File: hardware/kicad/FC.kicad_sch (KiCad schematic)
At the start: 0 parts

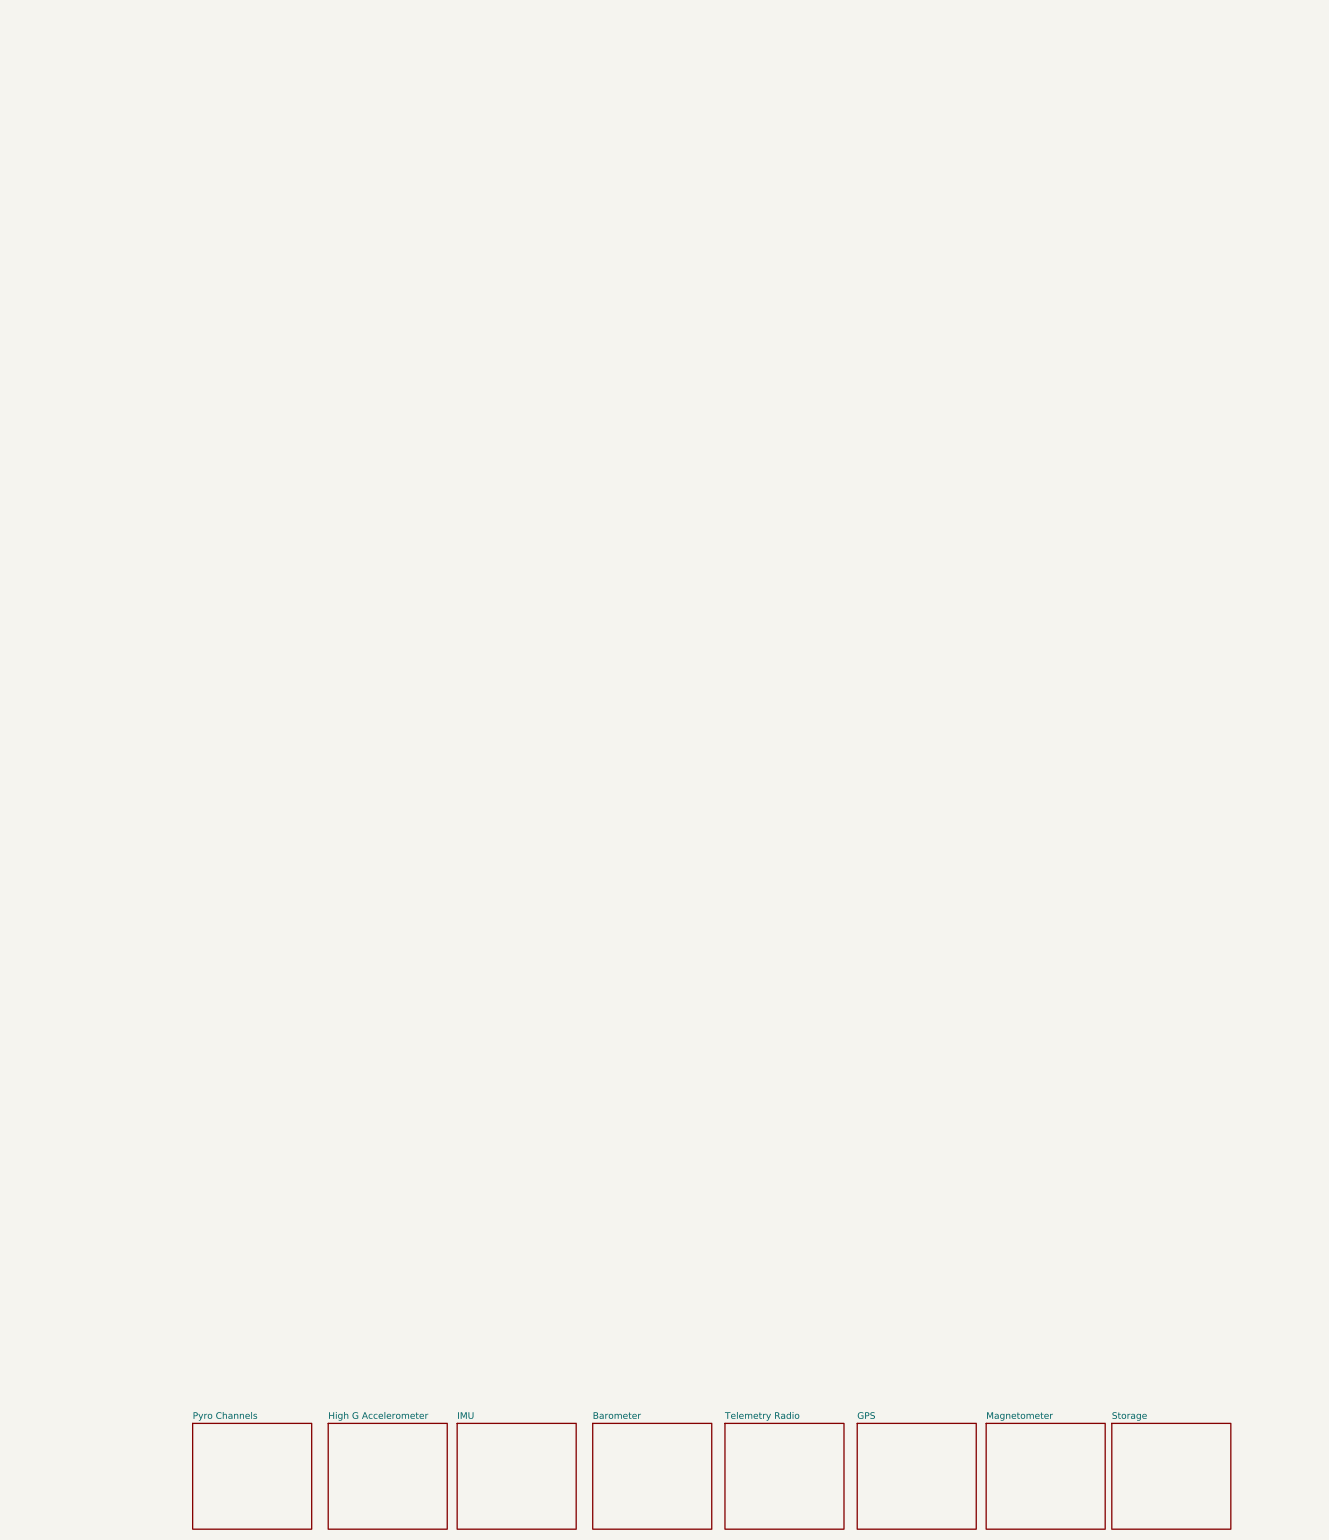
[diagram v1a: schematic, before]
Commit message: created microcontroller schematic
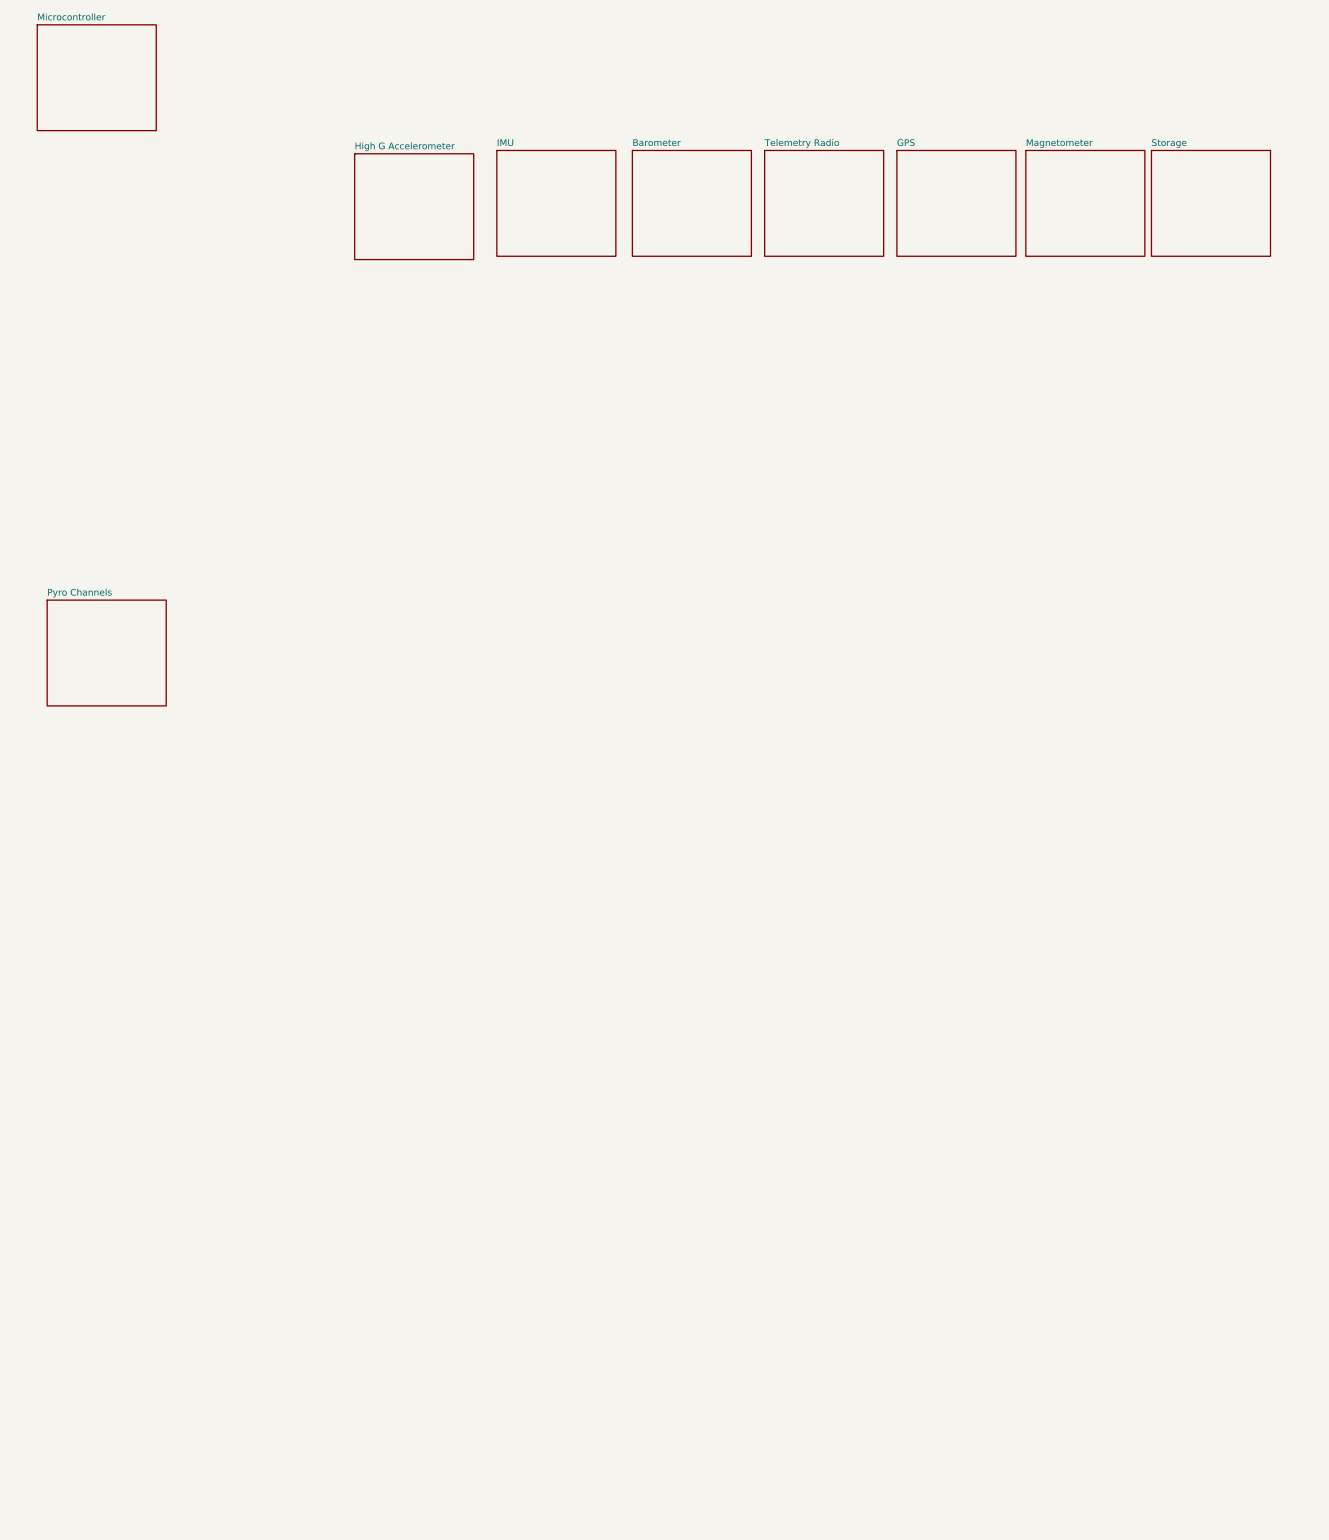
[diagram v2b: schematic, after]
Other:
- added sheet Microcontroller (hierarchical_sheets/atmega32u4.kicad_sch)
- company: (none) -> Missouri S&T Rocket Design Team
- title: (none) -> SRAD-FC
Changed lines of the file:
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@@
 (kicad_sch (version 20230121) (generator eeschema)
-  (paper "A4")
-  (sheet (at 125.095 303.53) (size 22.86 20.32) (fields_autoplaced)
+  (paper "USLetter")
+  (title_block
+    (title "SRAD-FC")
+    (date "2023-09-16")
+    (company "Missouri S&T Rocket Design Team")
+  )
+  (sheet (at 132.715 59.055) (size 22.86 20.32) (fields_autoplaced)
     (stroke (width 0.1524) (type solid))
     (fill (color 255 255 194 1.0000))
-    (property "Sheetname" "Barometer" (at 125.095 302.8184 0)
+    (property "Sheetname" "Barometer" (at 132.715 58.3434 0)
       (effects (font (size 1.27 1.27)) (justify left bottom))
     )
-    (property "Sheetfile" "hierarchical_sheets/ms5611.kicad_sch" (at 125.095 324.4346 0)
+    (property "Sheetfile" "hierarchical_sheets/ms5611.kicad_sch" (at 132.715 79.9596 0)
       (effects (font (size 1.27 1.27)) (justify left top) hide)
     )
@@
     )
   )
-  (sheet (at 48.26 303.53) (size 22.86 20.32) (fields_autoplaced)
+  (sheet (at 20.32 145.415) (size 22.86 20.32) (fields_autoplaced)
     (stroke (width 0.1524) (type solid))
     (fill (color 255 255 194 1.0000))
-    (property "Sheetname" "Pyro Channels" (at 48.26 302.8184 0)
+    (property "Sheetname" "Pyro Channels" (at 20.32 144.7034 0)
       (effects (font (size 1.27 1.27)) (justify left bottom))
     )
-    (property "Sheetfile" "hierarchical_sheets/pyro_channel.kicad_sch" (at 48.26 324.4346 0)
+    (property "Sheetfile" "hierarchical_sheets/pyro_channel.kicad_sch" (at 20.32 166.3196 0)
       (effects (font (size 1.27 1.27)) (justify left top) hide)
     )
@@
     )
   )
-  (sheet (at 150.495 303.53) (size 22.86 20.32) (fields_autoplaced)
+  (sheet (at 158.115 59.055) (size 22.86 20.32) (fields_autoplaced)
     (stroke (width 0.1524) (type solid))
     (fill (color 255 255 194 1.0000))
-    (property "Sheetname" "Telemetry Radio" (at 150.495 302.8184 0)
+    (property "Sheetname" "Telemetry Radio" (at 158.115 58.3434 0)
       (effects (font (size 1.27 1.27)) (justify left bottom))
     )
-    (property "Sheetfile" "hierarchical_sheets/ra-01sh.kicad_sch" (at 150.495 324.4346 0)
+    (property "Sheetfile" "hierarchical_sheets/ra-01sh.kicad_sch" (at 158.115 79.9596 0)
       (effects (font (size 1.27 1.27)) (justify left top) hide)
     )
@@
     )
   )
-  (sheet (at 200.66 303.53) (size 22.86 20.32) (fields_autoplaced)
+  (sheet (at 208.28 59.055) (size 22.86 20.32) (fields_autoplaced)
     (stroke (width 0.1524) (type solid))
     (fill (color 255 255 194 1.0000))
-    (property "Sheetname" "Magnetometer" (at 200.66 302.8184 0)
+    (property "Sheetname" "Magnetometer" (at 208.28 58.3434 0)
       (effects (font (size 1.27 1.27)) (justify left bottom))
     )
-    (property "Sheetfile" "hierarchical_sheets/bmm-350.kicad_sch" (at 200.66 324.4346 0)
+    (property "Sheetfile" "hierarchical_sheets/bmm-350.kicad_sch" (at 208.28 79.9596 0)
       (effects (font (size 1.27 1.27)) (justify left top) hide)
     )
@@
     )
   )
-  (sheet (at 99.06 303.53) (size 22.86 20.32) (fields_autoplaced)
+  (sheet (at 106.68 59.055) (size 22.86 20.32) (fields_autoplaced)
     (stroke (width 0.1524) (type solid))
     (fill (color 255 255 194 1.0000))
-    (property "Sheetname" "IMU" (at 99.06 302.8184 0)
+    (property "Sheetname" "IMU" (at 106.68 58.3434 0)
       (effects (font (size 1.27 1.27)) (justify left bottom))
     )
-    (property "Sheetfile" "hierarchical_sheets/bmi-270.kicad_sch" (at 99.06 324.4346 0)
+    (property "Sheetfile" "hierarchical_sheets/bmi-270.kicad_sch" (at 106.68 79.9596 0)
       (effects (font (size 1.27 1.27)) (justify left top) hide)
     )
@@
     )
   )
-  (sheet (at 74.295 303.53) (size 22.86 20.32) (fields_autoplaced)
+  (sheet (at 18.415 34.925) (size 22.86 20.32) (fields_autoplaced)
     (stroke (width 0.1524) (type solid))
     (fill (color 255 255 194 1.0000))
-    (property "Sheetname" "High G Accelerometer" (at 74.295 302.8184 0)
+    (property "Sheetname" "Microcontroller" (at 18.415 34.2134 0)
       (effects (font (size 1.27 1.27)) (justify left bottom))
     )
-    (property "Sheetfile" "hierarchical_sheets/kx134-1211.kicad_sch" (at 74.295 324.4346 0)
+    (property "Sheetfile" "hierarchical_sheets/atmega32u4.kicad_sch" (at 18.415 55.8296 0)
+      (effects (font (size 1.27 1.27)) (justify left top) hide)
+    )
+    (instances
+      (project "FC"
+        (path "/54cce219-8b98-4e71-96c4-f9ee784aa3bc" (page "10"))
+      )
+    )
+  )
+  (sheet (at 79.375 59.69) (size 22.86 20.32) (fields_autoplaced)
+    (stroke (width 0.1524) (type solid))
+    (fill (color 255 255 194 1.0000))
+    (property "Sheetname" "High G Accelerometer" (at 79.375 58.9784 0)
+      (effects (font (size 1.27 1.27)) (justify left bottom))
+    )
+    (property "Sheetfile" "hierarchical_sheets/kx134-1211.kicad_sch" (at 79.375 80.5946 0)
       (effects (font (size 1.27 1.27)) (justify left top) hide)
     )
@@
     )
   )
-  (sheet (at 224.79 303.53) (size 22.86 20.32) (fields_autoplaced)
+  (sheet (at 232.41 59.055) (size 22.86 20.32) (fields_autoplaced)
     (stroke (width 0.1524) (type solid))
     (fill (color 255 255 194 1.0000))
-    (property "Sheetname" "Storage" (at 224.79 302.8184 0)
+    (property "Sheetname" "Storage" (at 232.41 58.3434 0)
       (effects (font (size 1.27 1.27)) (justify left bottom))
     )
-    (property "Sheetfile" "hierarchical_sheets/mb85rs2mtapnf.kicad_sch" (at 224.79 324.4346 0)
+    (property "Sheetfile" "hierarchical_sheets/mb85rs2mtapnf.kicad_sch" (at 232.41 79.9596 0)
       (effects (font (size 1.27 1.27)) (justify left top) hide)
     )
@@
     )
   )
-  (sheet (at 175.895 303.53) (size 22.86 20.32) (fields_autoplaced)
+  (sheet (at 183.515 59.055) (size 22.86 20.32) (fields_autoplaced)
     (stroke (width 0.1524) (type solid))
     (fill (color 255 255 194 1.0000))
-    (property "Sheetname" "GPS" (at 175.895 302.8184 0)
+    (property "Sheetname" "GPS" (at 183.515 58.3434 0)
       (effects (font (size 1.27 1.27)) (justify left bottom))
     )
-    (property "Sheetfile" "hierarchical_sheets/m10s.kicad_sch" (at 175.895 324.4346 0)
+    (property "Sheetfile" "hierarchical_sheets/m10s.kicad_sch" (at 183.515 79.9596 0)
       (effects (font (size 1.27 1.27)) (justify left top) hide)
     )

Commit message: assigned schematics
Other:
- note added: "Skye: High G Accelerometer - (kx134-1211) Ben: Barometer - (ms5611) Riley: GPS -(m10s) Sean Duda: Magnetometer - (bmm350) Ariel: Telemetry Radio - (Ra-01SH) Clifford: Storage (MB85RS2MTAPNF) Evan: IMU (BMI-270)"
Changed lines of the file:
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@@
     (company "Missouri S&T Rocket Design Team")
   )
-  (sheet (at 132.715 59.055) (size 22.86 20.32) (fields_autoplaced)
+  (text "Skye: High G Accelerometer - (kx134-1211)\nBen: Barometer - (ms5611)\nRiley: GPS -(m10s)\nSean Duda: Magnetometer - (bmm350)\nAriel: Telemetry Radio - (Ra-01SH)\nClifford: Storage (MB85RS2MTAPNF)\nEvan: IMU (BMI-270)\n"
+    (at 158.75 160.02 0)
+    (effects (font (size 2.56 2.56) (thickness 0.512) bold) (justify left bottom))
+  )
+  (sheet (at 127 35.56) (size 22.86 20.32) (fields_autoplaced)
     (stroke (width 0.1524) (type solid))
     (fill (color 255 255 194 1.0000))
-    (property "Sheetname" "Barometer" (at 132.715 58.3434 0)
+    (property "Sheetname" "Barometer" (at 127 34.8484 0)
       (effects (font (size 1.27 1.27)) (justify left bottom))
     )
-    (property "Sheetfile" "hierarchical_sheets/ms5611.kicad_sch" (at 132.715 79.9596 0)
+    (property "Sheetfile" "hierarchical_sheets/ms5611.kicad_sch" (at 127 56.4646 0)
       (effects (font (size 1.27 1.27)) (justify left top) hide)
     )
@@
     )
   )
-  (sheet (at 20.32 145.415) (size 22.86 20.32) (fields_autoplaced)
+  (sheet (at 13.335 172.72) (size 22.86 20.32) (fields_autoplaced)
     (stroke (width 0.1524) (type solid))
     (fill (color 255 255 194 1.0000))
-    (property "Sheetname" "Pyro Channels" (at 20.32 144.7034 0)
+    (property "Sheetname" "Pyro Channels" (at 13.335 172.0084 0)
       (effects (font (size 1.27 1.27)) (justify left bottom))
     )
-    (property "Sheetfile" "hierarchical_sheets/pyro_channel.kicad_sch" (at 20.32 166.3196 0)
+    (property "Sheetfile" "hierarchical_sheets/pyro_channel.kicad_sch" (at 13.335 193.6246 0)
       (effects (font (size 1.27 1.27)) (justify left top) hide)
     )
@@
     )
   )
-  (sheet (at 158.115 59.055) (size 22.86 20.32) (fields_autoplaced)
+  (sheet (at 153.67 34.925) (size 22.86 20.32) (fields_autoplaced)
     (stroke (width 0.1524) (type solid))
     (fill (color 255 255 194 1.0000))
-    (property "Sheetname" "Telemetry Radio" (at 158.115 58.3434 0)
+    (property "Sheetname" "Telemetry Radio" (at 153.67 34.2134 0)
       (effects (font (size 1.27 1.27)) (justify left bottom))
     )
-    (property "Sheetfile" "hierarchical_sheets/ra-01sh.kicad_sch" (at 158.115 79.9596 0)
+    (property "Sheetfile" "hierarchical_sheets/ra-01sh.kicad_sch" (at 153.67 55.8296 0)
       (effects (font (size 1.27 1.27)) (justify left top) hide)
     )
@@
     )
   )
-  (sheet (at 208.28 59.055) (size 22.86 20.32) (fields_autoplaced)
+  (sheet (at 203.835 34.925) (size 22.86 20.32) (fields_autoplaced)
     (stroke (width 0.1524) (type solid))
     (fill (color 255 255 194 1.0000))
-    (property "Sheetname" "Magnetometer" (at 208.28 58.3434 0)
+    (property "Sheetname" "Magnetometer" (at 203.835 34.2134 0)
       (effects (font (size 1.27 1.27)) (justify left bottom))
     )
-    (property "Sheetfile" "hierarchical_sheets/bmm-350.kicad_sch" (at 208.28 79.9596 0)
+    (property "Sheetfile" "hierarchical_sheets/bmm-350.kicad_sch" (at 203.835 55.8296 0)
       (effects (font (size 1.27 1.27)) (justify left top) hide)
     )
@@
     )
   )
-  (sheet (at 106.68 59.055) (size 22.86 20.32) (fields_autoplaced)
+  (sheet (at 102.235 35.56) (size 22.86 20.32) (fields_autoplaced)
     (stroke (width 0.1524) (type solid))
     (fill (color 255 255 194 1.0000))
-    (property "Sheetname" "IMU" (at 106.68 58.3434 0)
+    (property "Sheetname" "IMU" (at 102.235 34.8484 0)
       (effects (font (size 1.27 1.27)) (justify left bottom))
     )
-    (property "Sheetfile" "hierarchical_sheets/bmi-270.kicad_sch" (at 106.68 79.9596 0)
+    (property "Sheetfile" "hierarchical_sheets/bmi-270.kicad_sch" (at 102.235 56.4646 0)
       (effects (font (size 1.27 1.27)) (justify left top) hide)
     )
@@
     )
   )
-  (sheet (at 79.375 59.69) (size 22.86 20.32) (fields_autoplaced)
+  (sheet (at 78.105 35.56) (size 22.86 20.32) (fields_autoplaced)
     (stroke (width 0.1524) (type solid))
     (fill (color 255 255 194 1.0000))
-    (property "Sheetname" "High G Accelerometer" (at 79.375 58.9784 0)
+    (property "Sheetname" "High G Accelerometer" (at 78.105 34.8484 0)
       (effects (font (size 1.27 1.27)) (justify left bottom))
     )
-    (property "Sheetfile" "hierarchical_sheets/kx134-1211.kicad_sch" (at 79.375 80.5946 0)
+    (property "Sheetfile" "hierarchical_sheets/kx134-1211.kicad_sch" (at 78.105 56.4646 0)
       (effects (font (size 1.27 1.27)) (justify left top) hide)
     )
@@
     )
   )
-  (sheet (at 232.41 59.055) (size 22.86 20.32) (fields_autoplaced)
+  (sheet (at 230.505 34.925) (size 22.86 20.32) (fields_autoplaced)
     (stroke (width 0.1524) (type solid))
     (fill (color 255 255 194 1.0000))
-    (property "Sheetname" "Storage" (at 232.41 58.3434 0)
+    (property "Sheetname" "Storage" (at 230.505 34.2134 0)
       (effects (font (size 1.27 1.27)) (justify left bottom))
     )
-    (property "Sheetfile" "hierarchical_sheets/mb85rs2mtapnf.kicad_sch" (at 232.41 79.9596 0)
+    (property "Sheetfile" "hierarchical_sheets/mb85rs2mtapnf.kicad_sch" (at 230.505 55.8296 0)
       (effects (font (size 1.27 1.27)) (justify left top) hide)
     )
@@
     )
   )
-  (sheet (at 183.515 59.055) (size 22.86 20.32) (fields_autoplaced)
+  (sheet (at 179.07 34.925) (size 22.86 20.32) (fields_autoplaced)
     (stroke (width 0.1524) (type solid))
     (fill (color 255 255 194 1.0000))
-    (property "Sheetname" "GPS" (at 183.515 58.3434 0)
+    (property "Sheetname" "GPS" (at 179.07 34.2134 0)
       (effects (font (size 1.27 1.27)) (justify left bottom))
     )
-    (property "Sheetfile" "hierarchical_sheets/m10s.kicad_sch" (at 183.515 79.9596 0)
+    (property "Sheetfile" "hierarchical_sheets/m10s.kicad_sch" (at 179.07 55.8296 0)
       (effects (font (size 1.27 1.27)) (justify left top) hide)
     )

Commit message: Storage Updated
Didn't save. Added pins to hierarchal sheets. In/Out
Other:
- sheet Storage ports: added SCK, SI, SO, ~{CS}, ~{HOLD}, ~{WP}; removed none
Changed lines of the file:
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@@
     )
   )
-  (sheet (at 230.505 34.925) (size 22.86 20.32) (fields_autoplaced)
+  (sheet (at 237.49 34.925) (size 18.415 20.955) (fields_autoplaced)
     (stroke (width 0.1524) (type solid))
     (fill (color 255 255 194 1.0000))
-    (property "Sheetname" "Storage" (at 230.505 34.2134 0)
+    (property "Sheetname" "Storage" (at 237.49 34.2134 0)
       (effects (font (size 1.27 1.27)) (justify left bottom))
     )
-    (property "Sheetfile" "hierarchical_sheets/mb85rs2mtapnf.kicad_sch" (at 230.505 55.8296 0)
+    (property "Sheetfile" "hierarchical_sheets/mb85rs2mtapnf.kicad_sch" (at 237.49 56.4646 0)
       (effects (font (size 1.27 1.27)) (justify left top) hide)
     )
+    (pin "SCK" input (at 255.905 38.1 0)
+      (effects (font (size 1.27 1.27)) (justify right))
+    )
+    (pin "SO" output (at 237.49 45.72 180)
+      (effects (font (size 1.27 1.27)) (justify left))
+    )
+    (pin "SI" input (at 255.905 41.91 0)
+      (effects (font (size 1.27 1.27)) (justify right))
+    )
+    (pin "~{WP}" input (at 255.905 45.72 0)
+      (effects (font (size 1.27 1.27)) (justify right))
+    )
+    (pin "~{CS}" input (at 255.905 49.53 0)
+      (effects (font (size 1.27 1.27)) (justify right))
+    )
+    (pin "~{HOLD}" input (at 255.905 53.34 0)
+      (effects (font (size 1.27 1.27)) (justify right))
+    )
     (instances
